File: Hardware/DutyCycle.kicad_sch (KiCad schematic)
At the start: 42 parts, among them J1 LiPo, J2 USB, J4 MOT, Q1 AO3400A, Q2 AO3400A, Q3 AO3401A, SW1 SW_Push, U1 AT32F421KxU7, U3 ME6211C28M5, U5 TP4055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

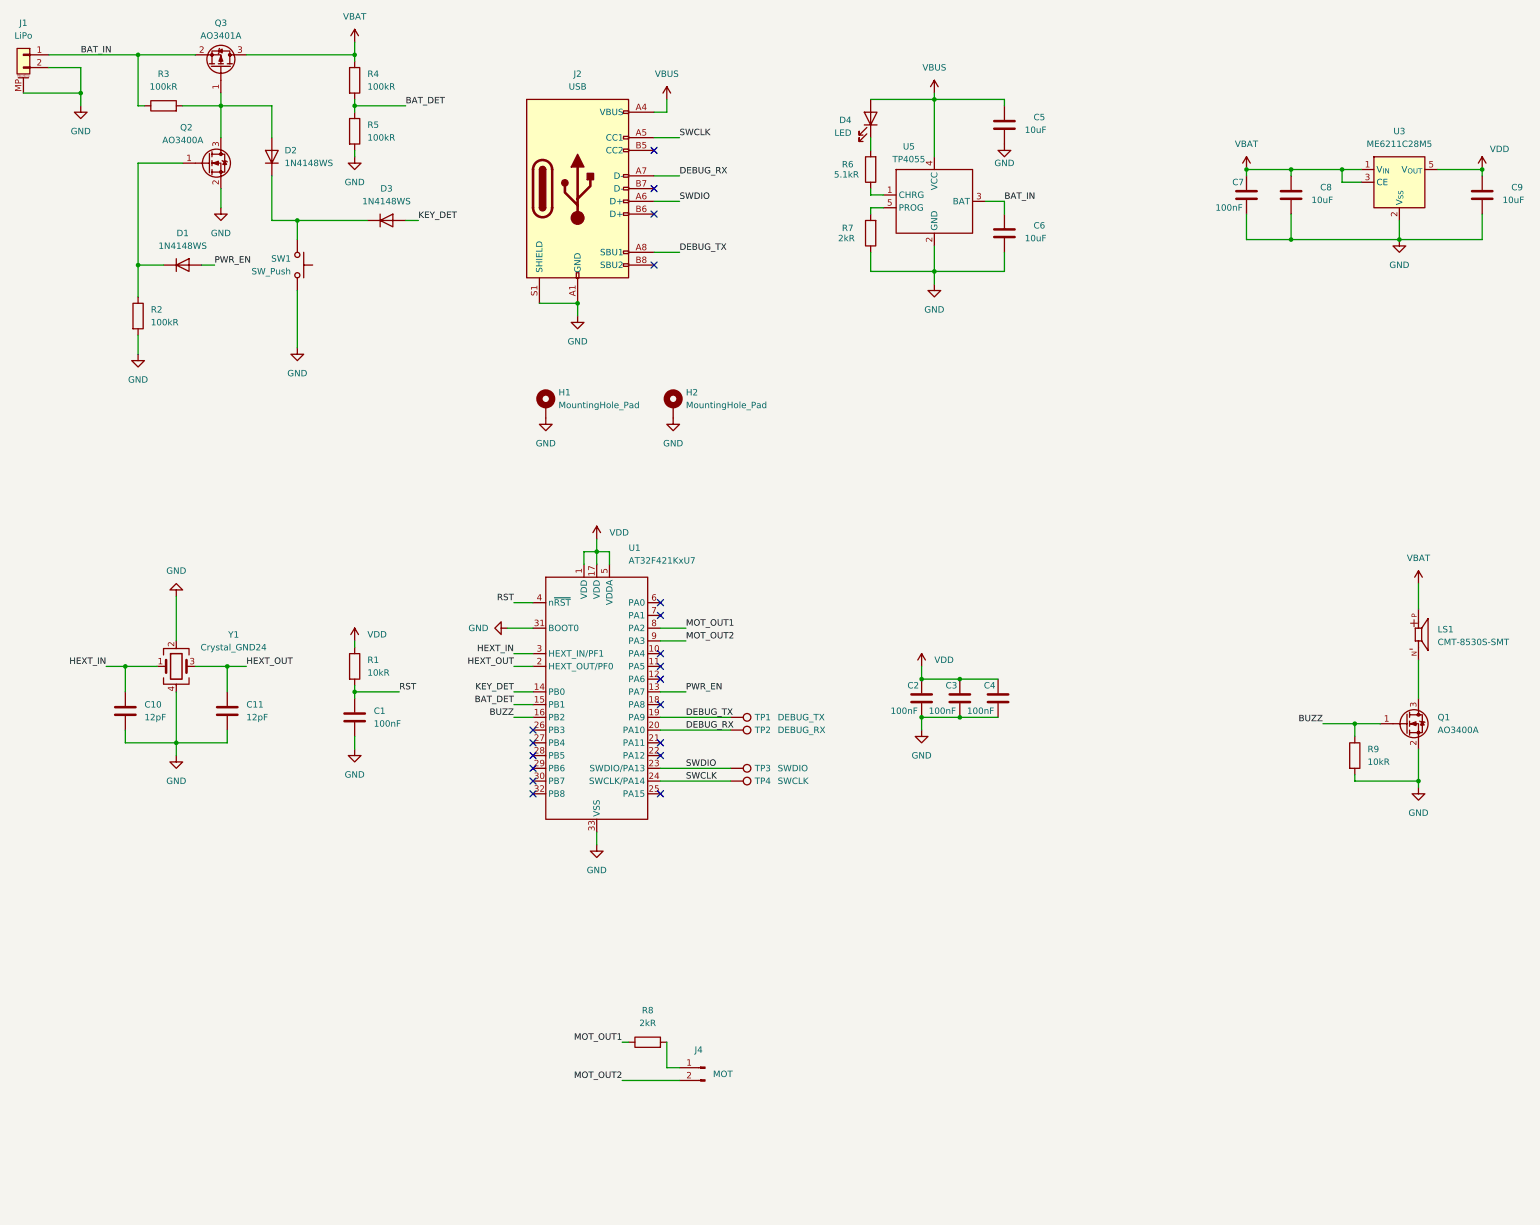
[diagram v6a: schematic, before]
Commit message: feat(Hardware): add CH340E
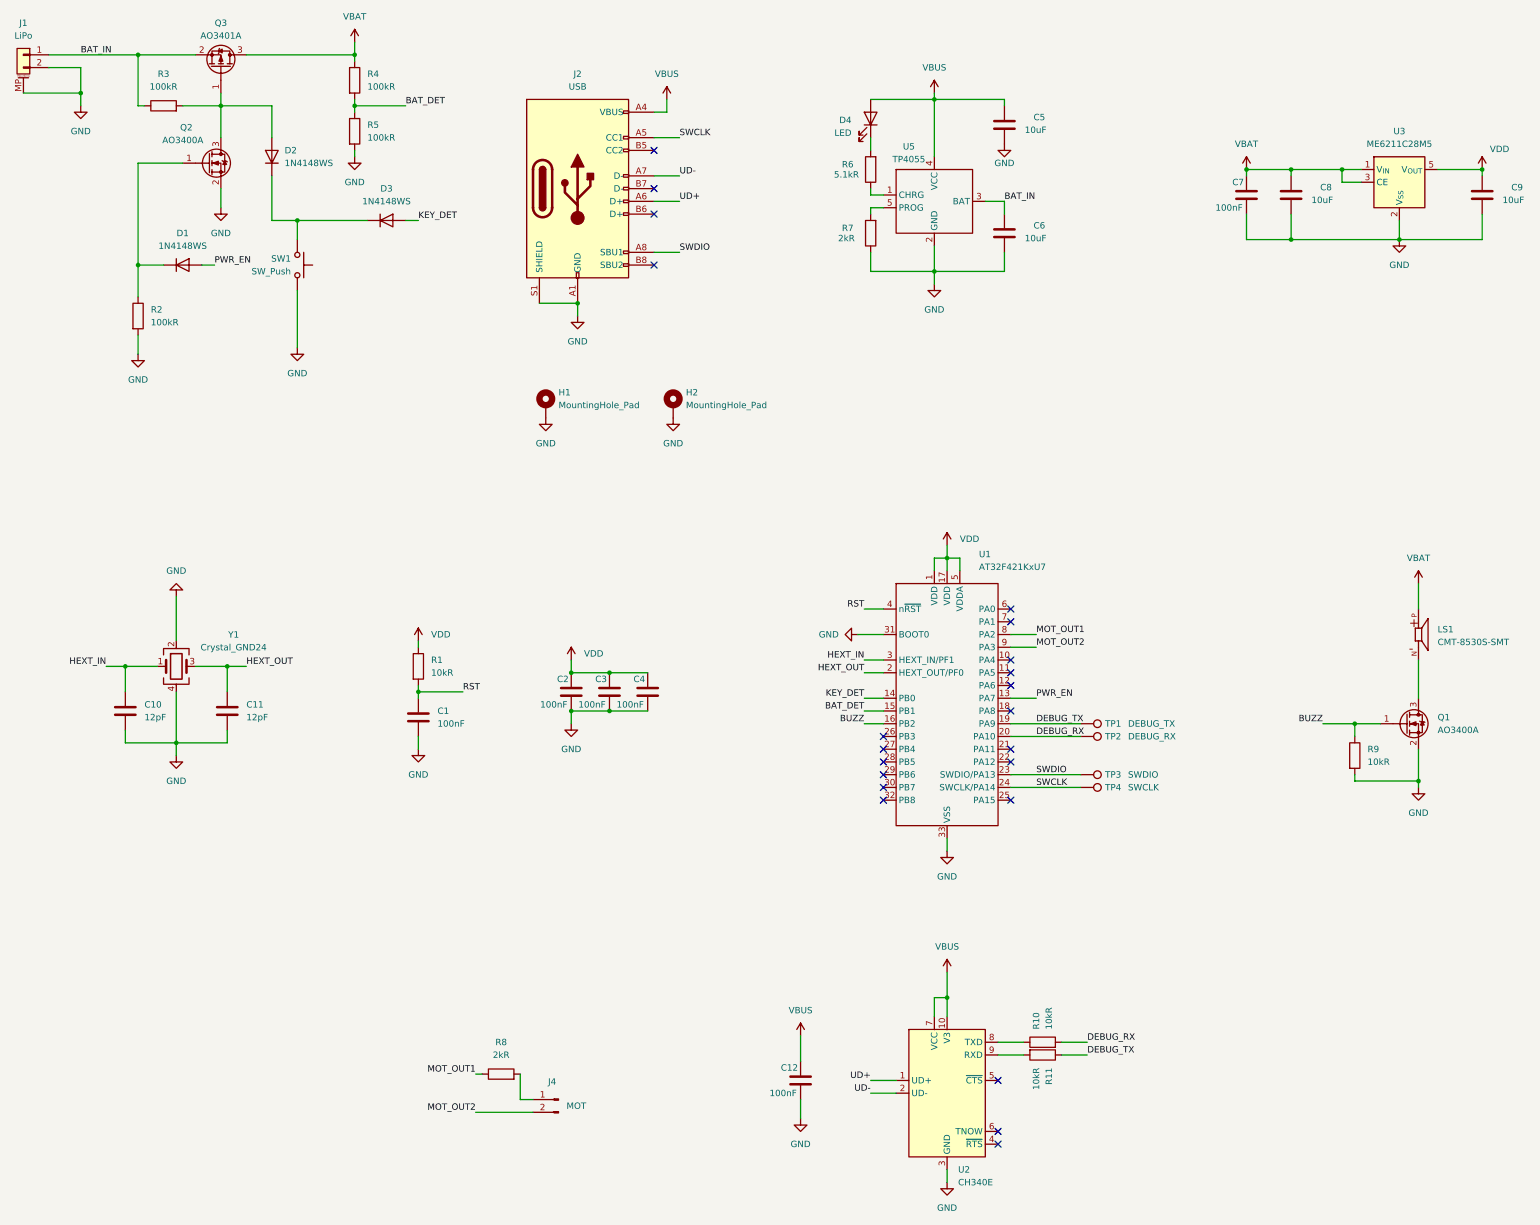
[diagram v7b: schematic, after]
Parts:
- added C12: 100nF, Capacitor_SMD:C_0402_1005Metric, symbol Device:C
- added R10, R11: 10kR, Resistor_SMD:R_0402_1005Metric, symbol Device:R
- added U2: CH340E, Package_SO:MSOP-10_3x3mm_P0.5mm, symbol Interface_USB:CH340E
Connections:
- net DEBUG_RX: now also R10.2; no longer J2.A7 (D-)
- net DEBUG_TX: now also R11.1; no longer J2.A8 (SBU1)
- net GND: now also C12.2, U2.3 (GND)
- net SWDIO: now also J2.A8 (SBU1); no longer J2.A6 (D+)
- net VBUS: now also C12.1, U2.10 (V3), U2.7 (VCC)
- new net: R10.1, U2.8 (TXD)
- new net: R11.2, U2.9 (RXD)
- new net UD+: J2.A6 (D+), U2.1 (UD+)
- new net UD-: J2.A7 (D-), U2.2 (UD-)
- no-connect marks 19 -> 22
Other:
- moved on the sheet: C1, C2, C3, C4, J4, R1, R8, TP1, TP2, TP3, TP4, U1

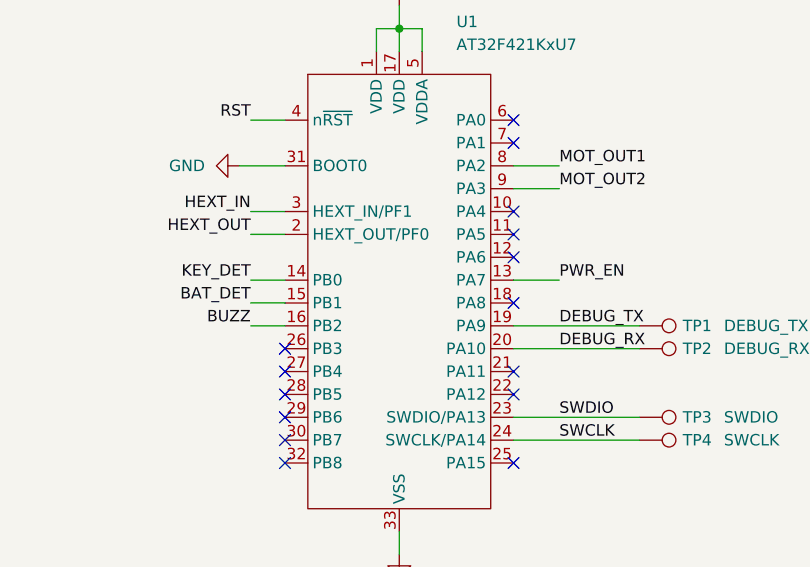
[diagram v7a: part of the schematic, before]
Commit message: fix(pcb): fix buzzer not connect to pwm pin
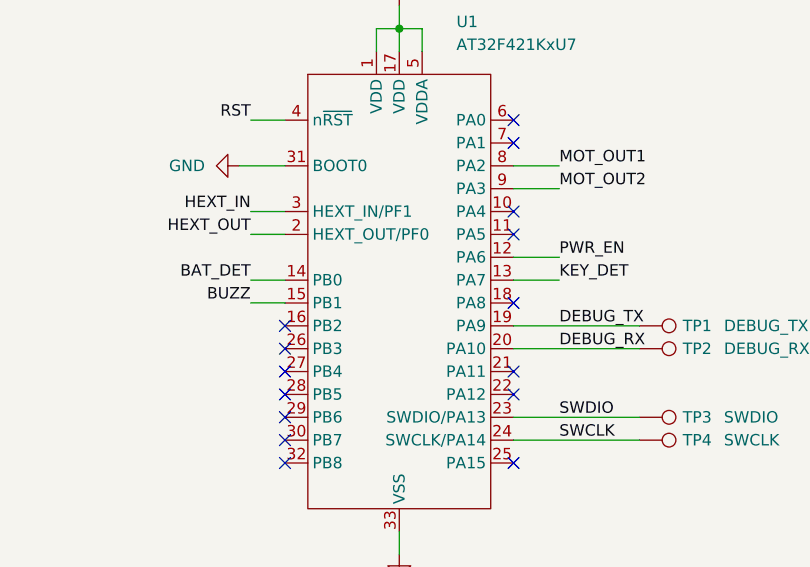
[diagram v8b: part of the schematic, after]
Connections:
- net BAT_DET: now also U1.14 (PB0); no longer U1.15 (PB1)
- net BUZZ: now also U1.15 (PB1); no longer U1.16 (PB2)
- net KEY_DET: now also U1.13 (PA7); no longer U1.14 (PB0)
- net PWR_EN: now also U1.12 (PA6); no longer U1.13 (PA7)
